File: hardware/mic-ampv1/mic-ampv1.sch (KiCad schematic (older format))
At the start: 16 parts, among them J1 XLR3_Switched, U1 NE5532

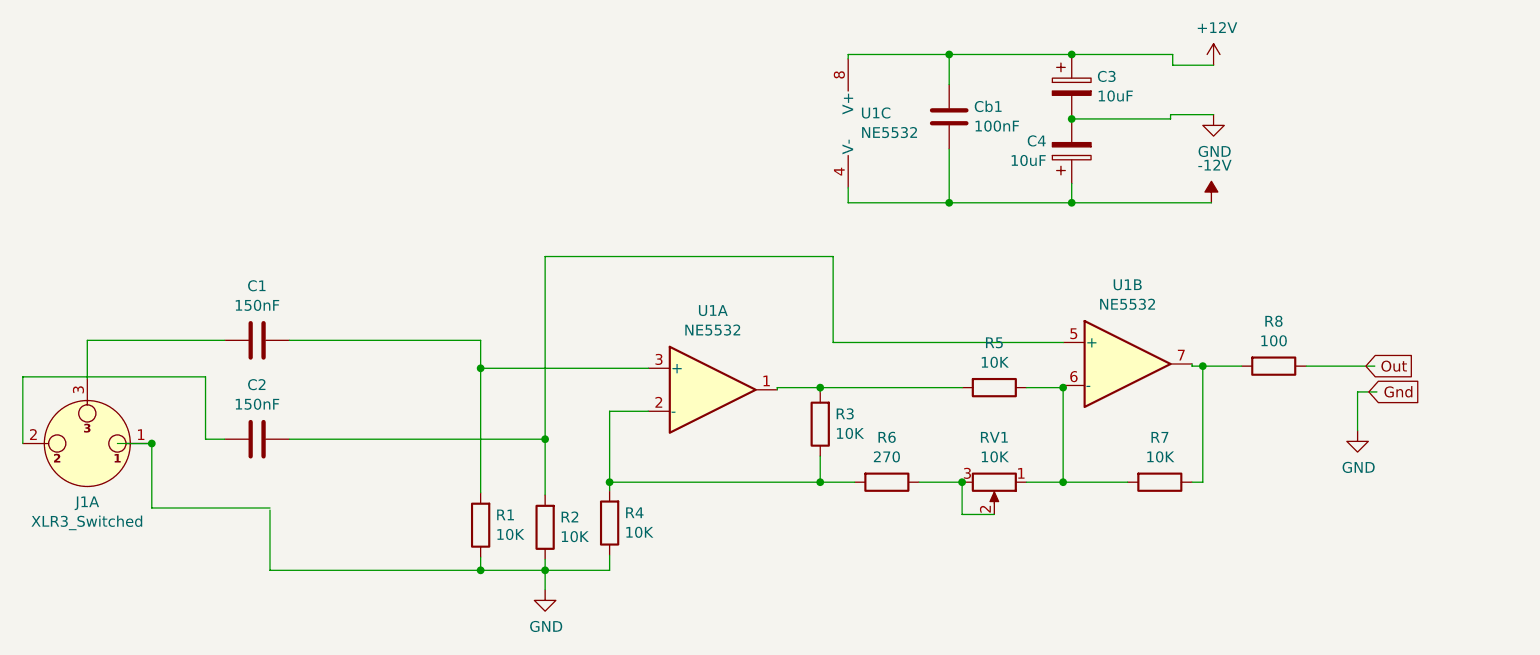
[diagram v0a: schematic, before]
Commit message: complete pcb for mic
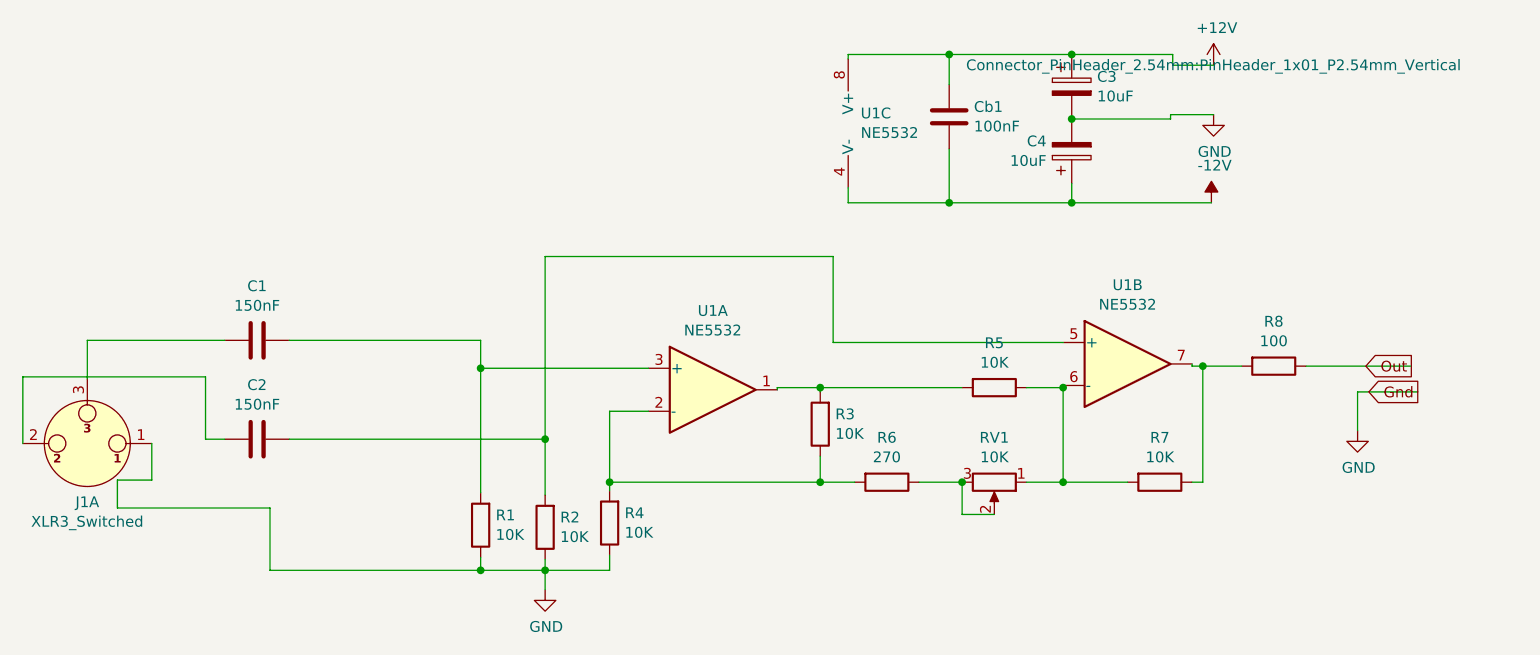
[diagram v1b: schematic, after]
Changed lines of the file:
@@
 Connection ~ 4640 3240
-Wire Wire Line
-	3660 4180 3660 3900
 Wire Wire Line
 	4640 4180 4940 4180
@@
 Wire Wire Line
 	7390 1780 6820 1780
-Wire Wire Line
-	6350 1780 6350 1800
 Connection ~ 7390 1780
 Wire Wire Line
@@
 Wire Wire Line
 	6820 2470 7390 2470
-Wire Wire Line
-	8810 3350 8720 3350
 Text GLabel 9000 3350 0    50   Output ~ 0
 Gnd
 Text GLabel 8970 3230 0    50   Output ~ 0
 Out
-Wire Wire Line
-	8480 3230 8800 3230
 Connection ~ 7390 2470
 Wire Wire Line
@@
 F 0 "#PWR0103" H 8050 1680 50  0001 C CNN
 F 1 "+12V" H 8065 2003 50  0000 C CNN
-F 2 "Connector_PinHeader_2.54mm:PinHeader_1x01_P2.54mm_Vertical" H 8050 1830 50  0001 C CNN
+F 2 "Connector_PinHeader_2.54mm:PinHeader_1x01_P2.54mm_Vertical" H 8050 1830 50  0000 C CNN
 F 3 "" H 8050 1830 50  0001 C CNN
 	1    8050 1830
 	1    0    0    -1
 $EndComp
-$Comp
-L Connector:XLR3_Switched J1
-U 1 1 680F40CD
-P 2810 3590
-F 0 "J1" H 2810 3863 50  0000 C CNN
-F 1 "XLR3_Switched" H 2810 3954 50  0000 C CNN
-F 2 "Connector_Audio:Jack_XLR-6.35mm_Neutrik_NCJ6FA-V-0_Vertical" H 2810 3690 50  0001 C CNN
-F 3 " ~" H 2810 3690 50  0001 C CNN
-	1    2810 3590
-	-1   0    0    1
-$EndComp
-Wire Wire Line
-	3660 3890 3110 3890
 Wire Wire Line
 	3450 3110 2810 3110
@@
 	3360 3570 3450 3570
 Wire Wire Line
-	2950 3590 3110 3590
+	8970 3230 8480 3230
 Wire Wire Line
-	3110 3890 3110 3590
+	9000 3350 8720 3350
 Wire Wire Line
-	3110 3590 3100 3590
-Connection ~ 3110 3590
+	3660 3890 3660 4180
+Wire Wire Line
+	2950 3890 2950 3760
+Wire Wire Line
+	2950 3890 3660 3890
+Wire Wire Line
+	6350 1800 6350 1780
+Wire Wire Line
+	3110 3590 3110 3760
+Wire Wire Line
+	3110 3760 2950 3760
+$Comp
+L Connector:XLR3_Switched J1
+U 1 1 680F40CD
+P 2810 3590
+F 0 "J1" H 2810 3863 50  0000 C CNN
+F 1 "XLR3_Switched" H 2810 3954 50  0000 C CNN
+F 2 "Connector_Audio:Jack_XLR-6.35mm_Neutrik_NCJ6FA-V-0_Vertical" H 2810 3690 50  0001 C CNN
+F 3 " ~" H 2810 3690 50  0001 C CNN
+	1    2810 3590
+	-1   0    0    1
+$EndComp
 $EndSCHEMATC
